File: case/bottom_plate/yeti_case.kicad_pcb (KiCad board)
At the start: 2 copper layers, 146.3 x 134.6 mm, 2 parts

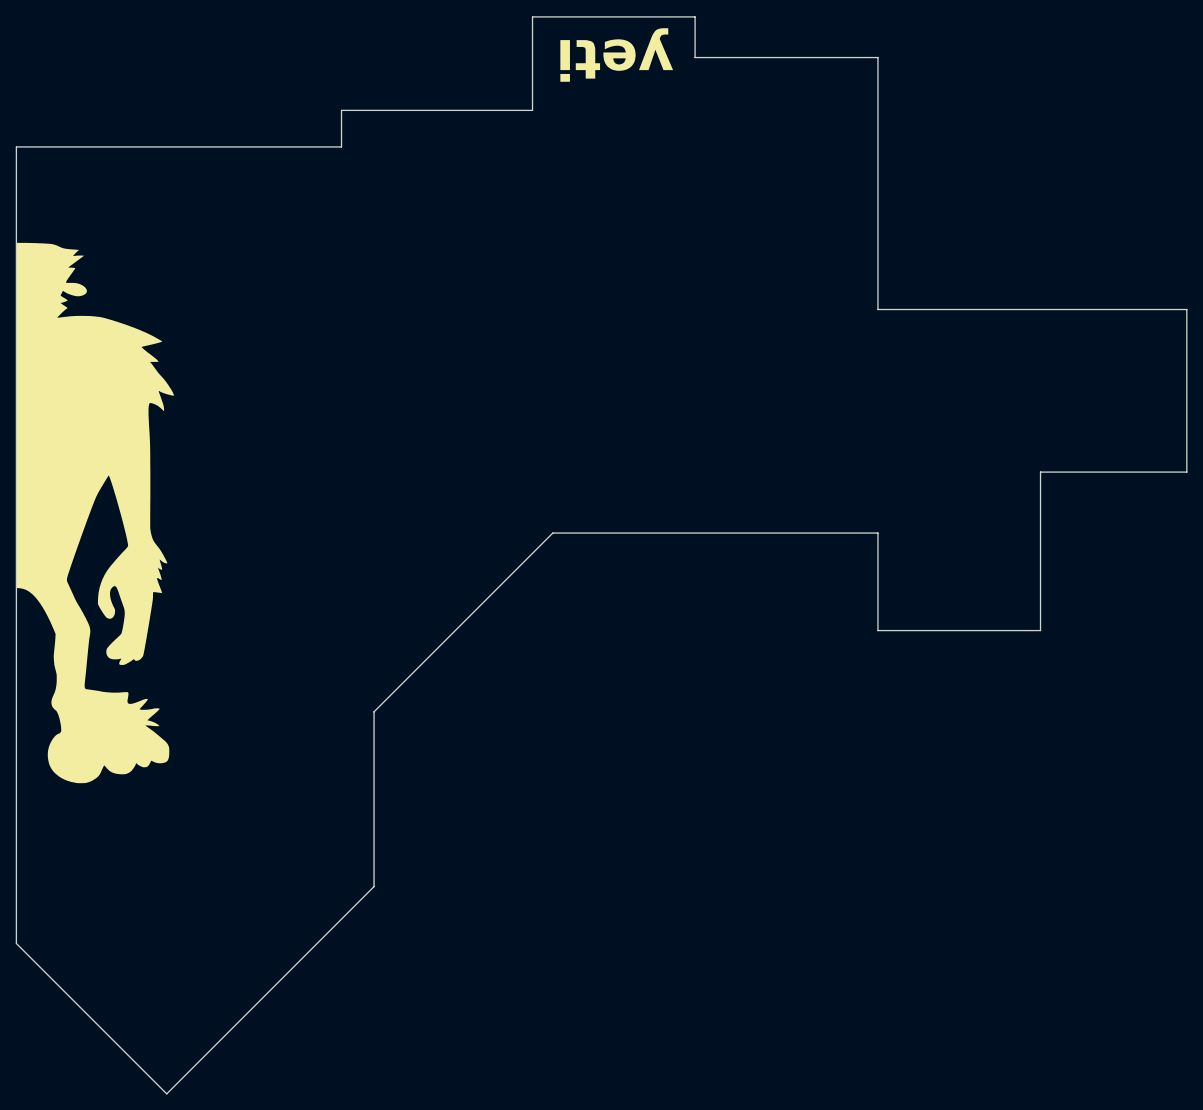
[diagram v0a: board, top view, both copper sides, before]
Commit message: case: Rearrange dirs and add top plate
Signed-off-by: Norbert Pocs <norbertpocs0@gmail.com>
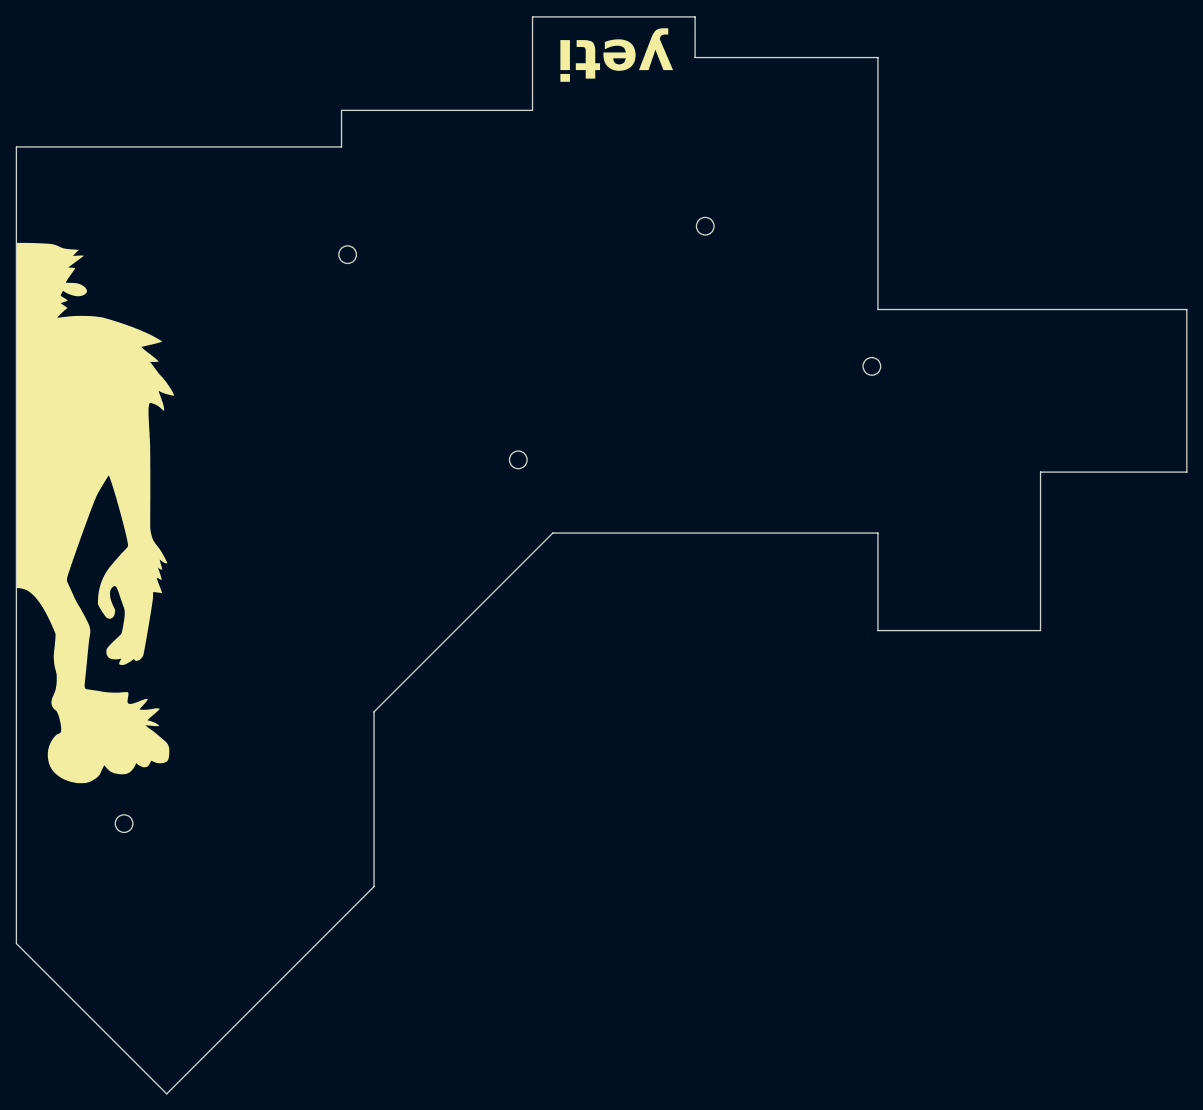
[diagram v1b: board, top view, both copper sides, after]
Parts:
- added REF**: MountingHole_2.2mm_M2_ISO7380, MountingHole:MountingHole_2.2mm_M2_ISO7380, F.Cu at (96.5, 131.8)
- added REF**: MountingHole_2.2mm_M2_ISO7380, MountingHole:MountingHole_2.2mm_M2_ISO7380, F.Cu at (124.5, 60.7)
- added REF**: MountingHole_2.2mm_M2_ISO7380, MountingHole:MountingHole_2.2mm_M2_ISO7380, F.Cu at (145.8, 86.4)
- added REF**: MountingHole_2.2mm_M2_ISO7380, MountingHole:MountingHole_2.2mm_M2_ISO7380, F.Cu at (169.2, 57.1)
- added REF**: MountingHole_2.2mm_M2_ISO7380, MountingHole:MountingHole_2.2mm_M2_ISO7380, F.Cu at (190.0, 74.7)
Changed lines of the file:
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@@
       (stroke (width 0) (type solid)) (fill solid) (layer "F.SilkS"))
+  )
+  (footprint "MountingHole:MountingHole_2.2mm_M2_ISO7380" (layer "F.Cu")
+    (at 96.52 131.826)
+    (descr "Mounting Hole 2.2mm, no annular, M2, ISO7380")
+    (tags "mounting hole 2.2mm no annular m2 iso7380")
+    (attr exclude_from_pos_files exclude_from_bom)
+    (fp_text reference "REF**" (at 0 -2.75) (layer "F.SilkS") hide
+        (effects (font (size 1 1) (thickness 0.15)))
+    )
+    (fp_text value "MountingHole_2.2mm_M2_ISO7380" (at 0 2.75) (layer "F.Fab") hide
+        (effects (font (size 1 1) (thickness 0.15)))
+    )
+    (fp_text user "${REFERENCE}" (at 0 0) (layer "F.Fab") hide
+        (effects (font (size 1 1) (thickness 0.15)))
+    )
+    (fp_circle (center 0 0) (end 1.75 0)
+      (stroke (width 0.15) (type solid)) (fill none) (layer "Cmts.User"))
+    (fp_circle (center 0 0) (end 2 0)
+      (stroke (width 0.05) (type solid)) (fill none) (layer "F.CrtYd"))
+    (pad "" np_thru_hole circle (at 0 0) (size 2.2 2.2) (drill 2.2) (layers "F&B.Cu" "*.Mask"))
+  )
+  (footprint "MountingHole:MountingHole_2.2mm_M2_ISO7380" (layer "F.Cu")
+    (at 124.46 60.706)
+    (descr "Mounting Hole 2.2mm, no annular, M2, ISO7380")
+    (tags "mounting hole 2.2mm no annular m2 iso7380")
+    (attr exclude_from_pos_files exclude_from_bom)
+    (fp_text reference "REF**" (at 0 -2.75) (layer "F.SilkS") hide
+        (effects (font (size 1 1) (thickness 0.15)))
+    )
+    (fp_text value "MountingHole_2.2mm_M2_ISO7380" (at 0 2.75) (layer "F.Fab") hide
+        (effects (font (size 1 1) (thickness 0.15)))
+    )
+    (fp_text user "${REFERENCE}" (at 0 0) (layer "F.Fab") hide
+        (effects (font (size 1 1) (thickness 0.15)))
+    )
+    (fp_circle (center 0 0) (end 1.75 0)
+      (stroke (width 0.15) (type solid)) (fill none) (layer "Cmts.User"))
+    (fp_circle (center 0 0) (end 2 0)
+      (stroke (width 0.05) (type solid)) (fill none) (layer "F.CrtYd"))
+    (pad "" np_thru_hole circle (at 0 0) (size 2.2 2.2) (drill 2.2) (layers "F&B.Cu" "*.Mask"))
+  )
+  (footprint "MountingHole:MountingHole_2.2mm_M2_ISO7380" (layer "F.Cu")
+    (at 145.796 86.36)
+    (descr "Mounting Hole 2.2mm, no annular, M2, ISO7380")
+    (tags "mounting hole 2.2mm no annular m2 iso7380")
+    (attr exclude_from_pos_files exclude_from_bom)
+    (fp_text reference "REF**" (at 0 -2.75) (layer "F.SilkS") hide
+        (effects (font (size 1 1) (thickness 0.15)))
+    )
+    (fp_text value "MountingHole_2.2mm_M2_ISO7380" (at 0 2.75) (layer "F.Fab") hide
+        (effects (font (size 1 1) (thickness 0.15)))
+    )
+    (fp_text user "${REFERENCE}" (at 0 0) (layer "F.Fab") hide
+        (effects (font (size 1 1) (thickness 0.15)))
+    )
+    (fp_circle (center 0 0) (end 1.75 0)
+      (stroke (width 0.15) (type solid)) (fill none) (layer "Cmts.User"))
+    (fp_circle (center 0 0) (end 2 0)
+      (stroke (width 0.05) (type solid)) (fill none) (layer "F.CrtYd"))
+    (pad "" np_thru_hole circle (at 0 0) (size 2.2 2.2) (drill 2.2) (layers "F&B.Cu" "*.Mask"))
   )
   (footprint "art:yeti_split_left" (layer "F.Cu")
@@
       (stroke (width 0) (type solid)) (fill solid) (layer "B.SilkS"))
   )
+  (footprint "MountingHole:MountingHole_2.2mm_M2_ISO7380" (layer "F.Cu")
+    (at 169.164 57.15)
+    (descr "Mounting Hole 2.2mm, no annular, M2, ISO7380")
+    (tags "mounting hole 2.2mm no annular m2 iso7380")
+    (attr exclude_from_pos_files exclude_from_bom)
+    (fp_text reference "REF**" (at 0 -2.75) (layer "F.SilkS") hide
+        (effects (font (size 1 1) (thickness 0.15)))
+    )
+    (fp_text value "MountingHole_2.2mm_M2_ISO7380" (at 0 2.75) (layer "F.Fab") hide
+        (effects (font (size 1 1) (thickness 0.15)))
+    )
+    (fp_text user "${REFERENCE}" (at 0 0) (layer "F.Fab") hide
+        (effects (font (size 1 1) (thickness 0.15)))
+    )
+    (fp_circle (center 0 0) (end 1.75 0)
+      (stroke (width 0.15) (type solid)) (fill none) (layer "Cmts.User"))
+    (fp_circle (center 0 0) (end 2 0)
+      (stroke (width 0.05) (type solid)) (fill none) (layer "F.CrtYd"))
+    (pad "" np_thru_hole circle (at 0 0) (size 2.2 2.2) (drill 2.2) (layers "F&B.Cu" "*.Mask"))
+  )
+  (footprint "MountingHole:MountingHole_2.2mm_M2_ISO7380" (layer "F.Cu")
+    (at 189.992 74.676)
+    (descr "Mounting Hole 2.2mm, no annular, M2, ISO7380")
+    (tags "mounting hole 2.2mm no annular m2 iso7380")
+    (attr exclude_from_pos_files exclude_from_bom)
+    (fp_text reference "REF**" (at 0 -2.75) (layer "F.SilkS") hide
+        (effects (font (size 1 1) (thickness 0.15)))
+    )
+    (fp_text value "MountingHole_2.2mm_M2_ISO7380" (at 0 2.75) (layer "F.Fab") hide
+        (effects (font (size 1 1) (thickness 0.15)))
+    )
+    (fp_text user "${REFERENCE}" (at 0 0) (layer "F.Fab") hide
+        (effects (font (size 1 1) (thickness 0.15)))
+    )
+    (fp_circle (center 0 0) (end 1.75 0)
+      (stroke (width 0.15) (type solid)) (fill none) (layer "Cmts.User"))
+    (fp_circle (center 0 0) (end 2 0)
+      (stroke (width 0.05) (type solid)) (fill none) (layer "F.CrtYd"))
+    (pad "" np_thru_hole circle (at 0 0) (size 2.2 2.2) (drill 2.2) (layers "F&B.Cu" "*.Mask"))
+  )
   (gr_line (start 167.894 30.988) (end 147.574 30.988)
